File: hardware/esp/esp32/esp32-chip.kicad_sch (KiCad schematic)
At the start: 27 parts, among them U12 ESP32-WROOM-32E(4MB), U3 SS8050_C2150, U8 SS8050_C2150

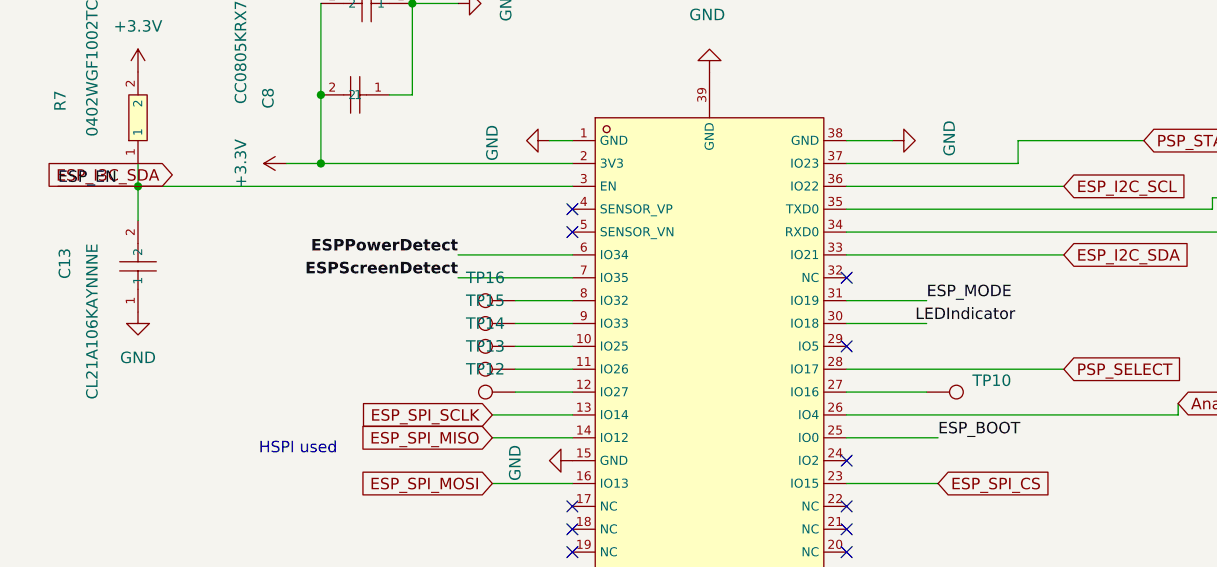
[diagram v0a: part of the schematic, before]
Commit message: Added hardware 0.2 - Added right FPC
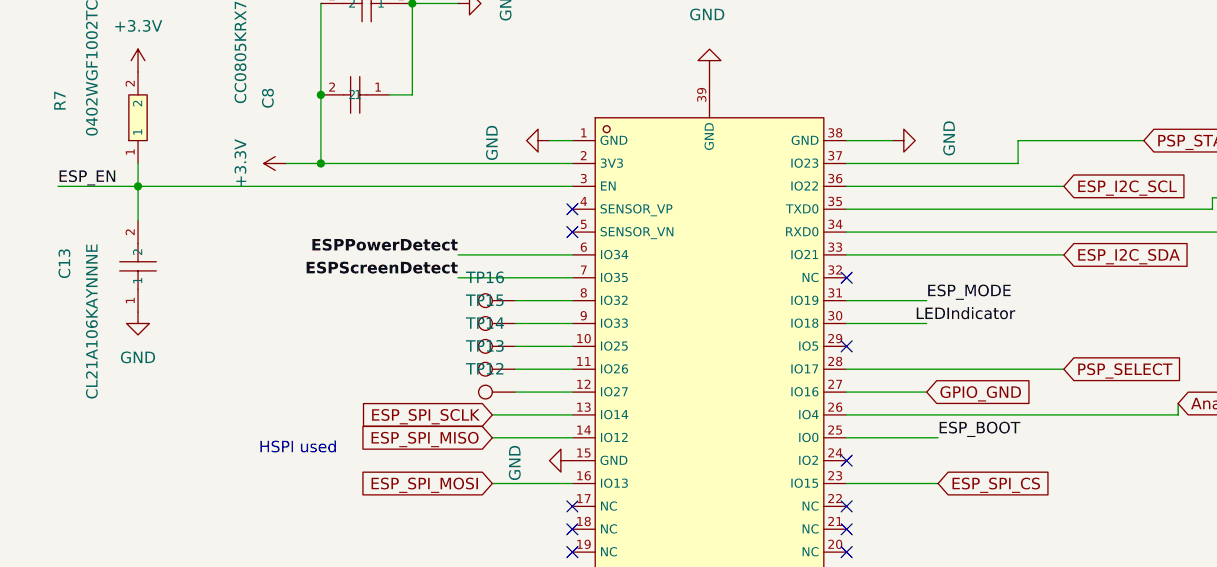
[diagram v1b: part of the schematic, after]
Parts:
- removed TP10: TestPoint, TestPoint:TestPoint_Pad_1.5x1.5mm, symbol Connector:TestPoint
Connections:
- net GPIO_GND: now reaches U12.27 (IO16)
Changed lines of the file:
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@@
+		)
+	)
+	(global_label "GPIO_GND"
+		(shape input)
+		(at 115.57 95.25 0)
+		(fields_autoplaced yes)
+		(effects
+			(font
+				(size 1.27 1.27)
+			)
+			(justify left)
+		)
+		(property "Intersheetrefs" "${INTERSHEET_REFS}"
+			(at 127.8686 95.25 0)
+			(effects
+				(font
+					(size 1.27 1.27)
+				)
+				(justify left)
+				(hide yes)
+			)
 		)
 	)
@@
 				)
 				(justify left)
-				(hide yes)
-			)
-		)
-	)
-	(global_label "ESP_I3C_SDA"
-		(shape input)
-		(at 31.75 71.12 180)
-		(fields_autoplaced yes)
-		(effects
-			(font
-				(size 1.27 1.27)
-			)
-			(justify right)
-		)
-		(property "Intersheetrefs" "${INTERSHEET_REFS}"
-			(at 16.5487 71.12 0)
-			(effects
-				(font
-					(size 1.27 1.27)
-				)
-				(justify right)
 				(hide yes)
 			)
@@
 					(unit 1)
 				)
-			)
-		)
-	)
-	(symbol
-		(lib_id "Connector:TestPoint")
-		(at 115.57 95.25 270)
-		(unit 1)
-		(exclude_from_sim no)
-		(in_bom yes)
-		(on_board yes)
-		(dnp no)
-		(fields_autoplaced yes)
-		(property "Reference" "TP10"
-			(at 120.65 93.9799 90)
-			(effects
-				(font
-					(size 1.27 1.27)
-				)
-				(justify left)
-			)
-		)
-		(property "Value" "TestPoint"
-			(at 120.65 96.5199 90)
-			(effects
-				(font
-					(size 1.27 1.27)
-				)
-				(justify left)
-				(hide yes)
-			)
-		)
-		(property "Footprint" "TestPoint:TestPoint_Pad_1.5x1.5mm"
-			(at 115.57 100.33 0)
-			(effects
-				(font
-					(size 1.27 1.27)
-				)
-				(hide yes)
-			)
-		)
-		(property "Datasheet" "~"
-			(at 115.57 100.33 0)
-			(effects
-				(font
-					(size 1.27 1.27)
-				)
-				(hide yes)
-			)
-		)
-		(property "Description" "test point"
-			(at 115.57 95.25 0)
-			(effects
-				(font
-					(size 1.27 1.27)
-				)
-				(hide yes)
-			)
-		)
-		(pin "1"
-		)
-		(instances
-			(project "esp32"
-				(path "/3a9f3299-35f4-4d62-9438-2986d1fa401f/4d61521e-d26b-4a87-9dc4-97977e5f7fed"
-					(reference "TP10")
-					(unit 1)
-				)

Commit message: stuff
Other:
- note added: "PSPPower and PSPScreen detect connect to PSP. Not found anywhere on the PSP itself that could expose such signals. But they are here ready"
- note removed: "PSPPower and PSPScreen detect connect to PSP."
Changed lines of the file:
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@@
 		)
 	)
-	(text "PSPPower and PSPScreen detect connect to PSP."
+	(text "PSPPower and PSPScreen detect connect to PSP.\nNot found anywhere on the PSP itself that could\nexpose such signals. But they are here ready"
 		(exclude_from_sim no)
 		(at 241.046 158.75 0)
